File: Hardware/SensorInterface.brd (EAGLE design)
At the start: 69 x 20 mm, 58 parts, among them J3 CONN_3SCREW_254, J4 CONN_3SCREW_254, J5 CONN_42.54_SCREW, Q1 DMG3404, Q2 2N7002, Q3 2N7002, Q4 DMG3404, Q5 DMG3404, U10 SN74AHC1G86DCK, U11 MCP6041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

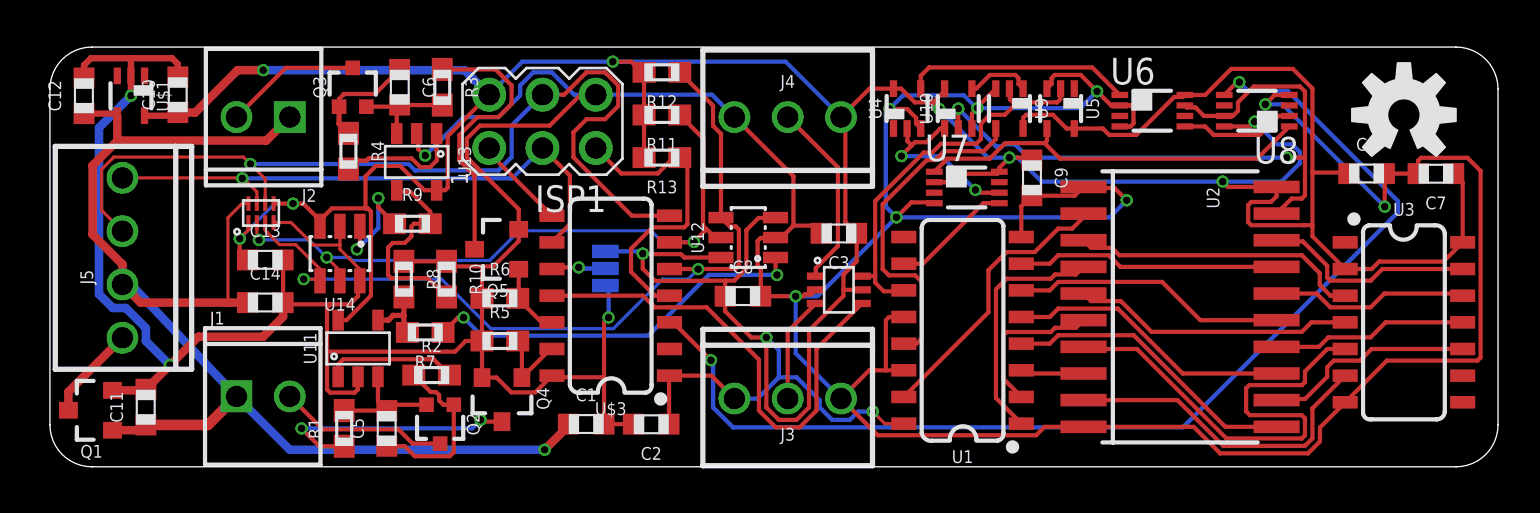
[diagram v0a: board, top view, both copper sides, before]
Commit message: thicker power path traces
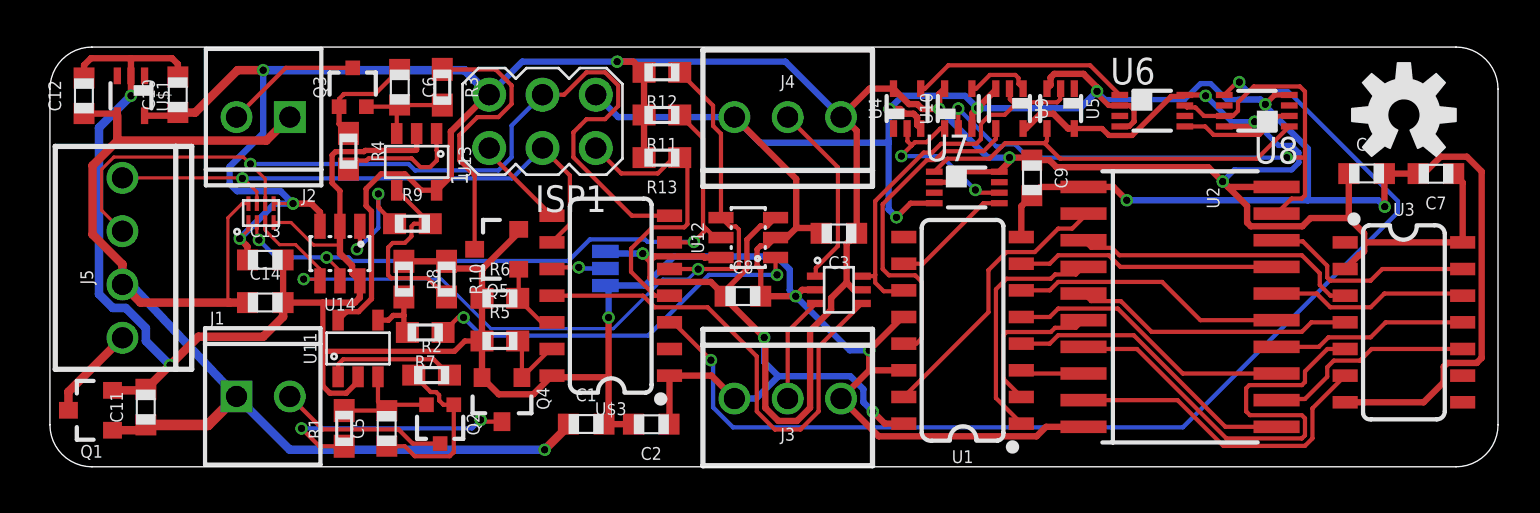
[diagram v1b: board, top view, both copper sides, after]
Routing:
- net GND: track 259.9 -> 248.7 mm
- net 3V3: track 211.6 -> 206.1 mm, vias 11 -> 12

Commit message: Added gerbers, minor cleanup, v0.0.0 submitted to fab
Cleaned up board and made some minor changes to decoupling capacitor layout, adjusted some traces. Generated gerbers and submitted boards for v0.0
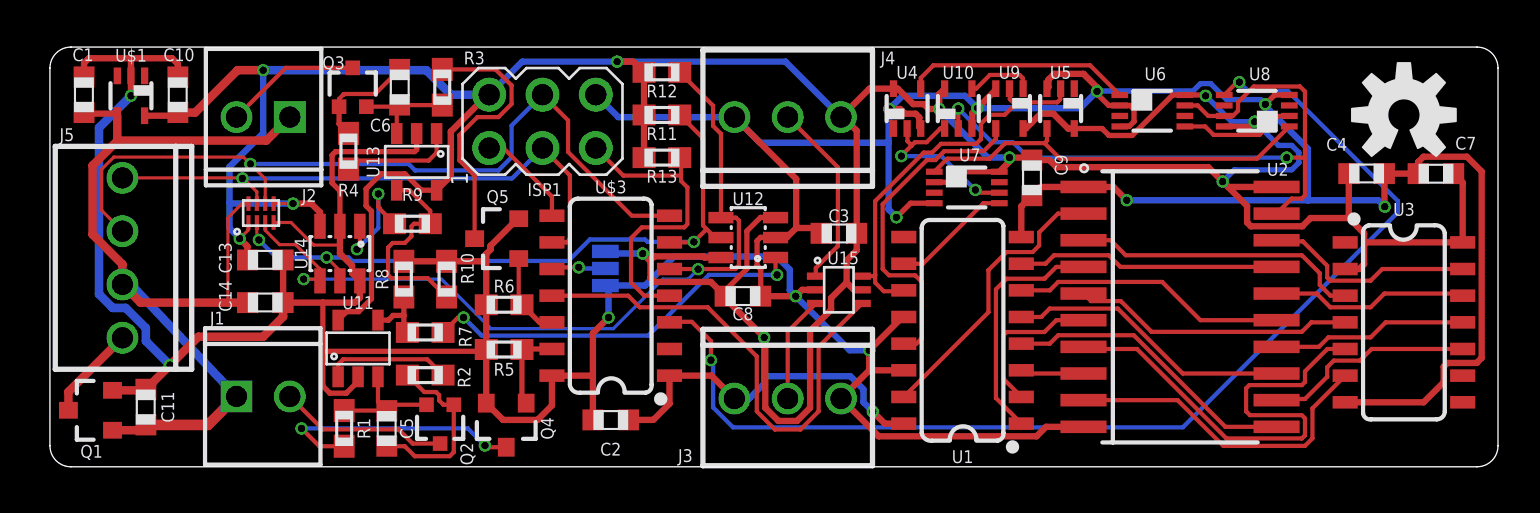
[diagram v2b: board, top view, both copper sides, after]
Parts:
- removed C12: 1uF, bschulz_passives:C0603
- J3, J4: value CONN_3SCREW_254 -> CONN_32.54_SCREW
- U6, U7, U8: device bschulz:DCU_(R-PDSO-G8)@1 -> bschulz:DCU_(R-PDSO-G8)
- moved C1 28.6 mm to (1.63, 17.7), turned to 90 degrees
- moved C2 1.94 mm to (26.7, 2.24)
- moved Q4 1.24 mm to (21.7, 2.03)
- moved Q5 0.51 mm to (21.3, 10.9)
- moved R5 0.45 mm to (21.6, 5.59)
- moved R6 0.37 mm to (21.6, 7.72)
- moved R2 0.30 mm to (17.9, 4.37)
- renumbered JP1 to JP0
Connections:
- net GND: no longer C12.2
- net VIN+: no longer C12.1
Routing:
- net VIN+: track 62.8 -> 45.4 mm, vias 1 -> 0
- net SDA_EXT: track 44.3 -> 38.8 mm
- net GND: track 248.7 -> 250.6 mm
- net 3V3: track 206.1 -> 207.3 mm
- net !RESET: track 14.7 -> 15.9 mm
- net LED2_CTRL: track 3.51 -> 4.26 mm
- net N$25: track 6.01 -> 5.43 mm
- net !INT: track 53.8 -> 54.3 mm
- net N$26: track 13.3 -> 12.8 mm
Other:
- outline, holes or cut-outs redrawn
- board text added: "3.3v ~ 5v"
- board text added: "JP0"
- board text added: "±"
- board text removed: "J0"

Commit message: Move and define caps
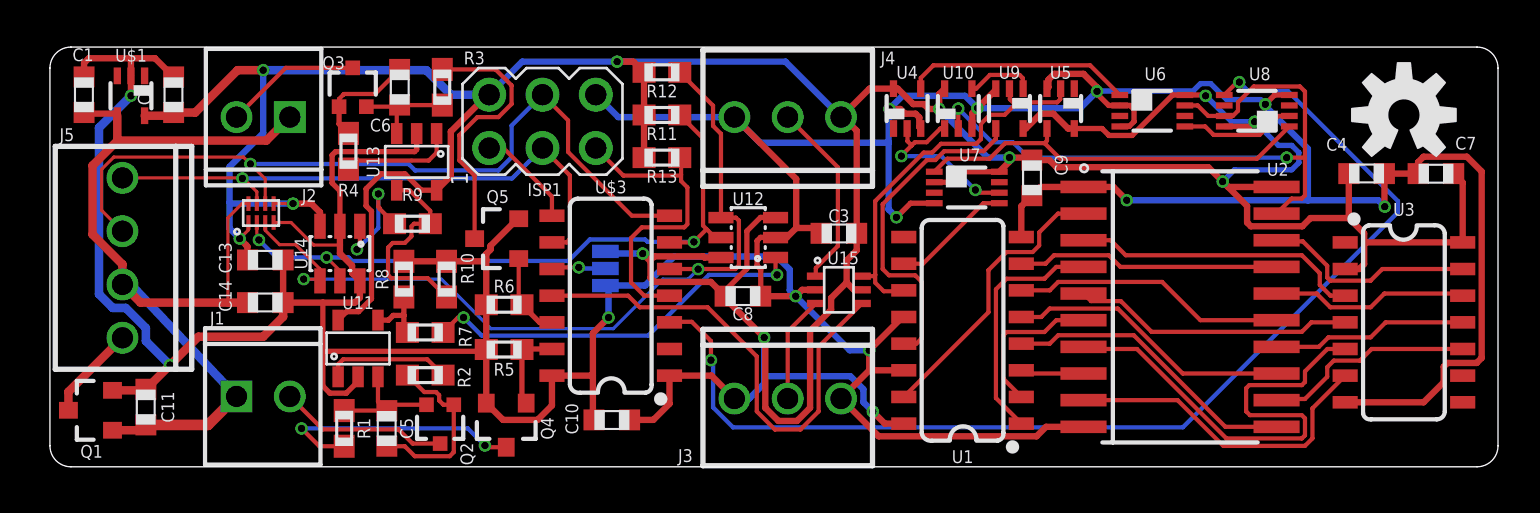
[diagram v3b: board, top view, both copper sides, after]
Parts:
- C1: value (none) -> 0.1uF
- C2: value (none) -> 1uF
- moved C2 26.0 mm to (5.89, 17.7), turned to 90 degrees
- moved C10 25.8 mm to (26.8, 2.24), turned to 180 degrees
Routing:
- net GND: track 250.6 -> 250.1 mm
